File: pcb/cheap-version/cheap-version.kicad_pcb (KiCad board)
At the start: 4 copper layers, 100 x 100 mm, 169 parts, among them J201 UART / 3V3 logic, J301 SHT4x / XH 2.50, J302 FLOAT / 3.5 mm, J401 HRO TF-01A, J501 FAN1 / 3.5 mm, J511 FAN2 / 3.5 mm, J521 PUMP 24V / 6W, J601 PTC + / switched - (3.5 mm), J711 LED +/- (return isolated), J721 LED +/- (return isolated), J731 LED +/- (return isolated), J901 24V IN (KF301-5.0-2P), Q501 AO3400A, Q511 AO3400A, Q521 AO3422, Q601 IRL2505, Q711 BSC146N10LS5, Q721 BSC146N10LS5, SW201 RESET, SW202 BOOT, U101 ST1S10PHR, U201 ESP32-WROOM-32E-N4, U301 PCF8563T/5, U601 UCC27524ADR, U700 SN74LVC1G08DBVR, U710 AL8853S-13, U720 AL8853S-13, U902 ST1S14PHR, Y301 32.768k 12.5pF

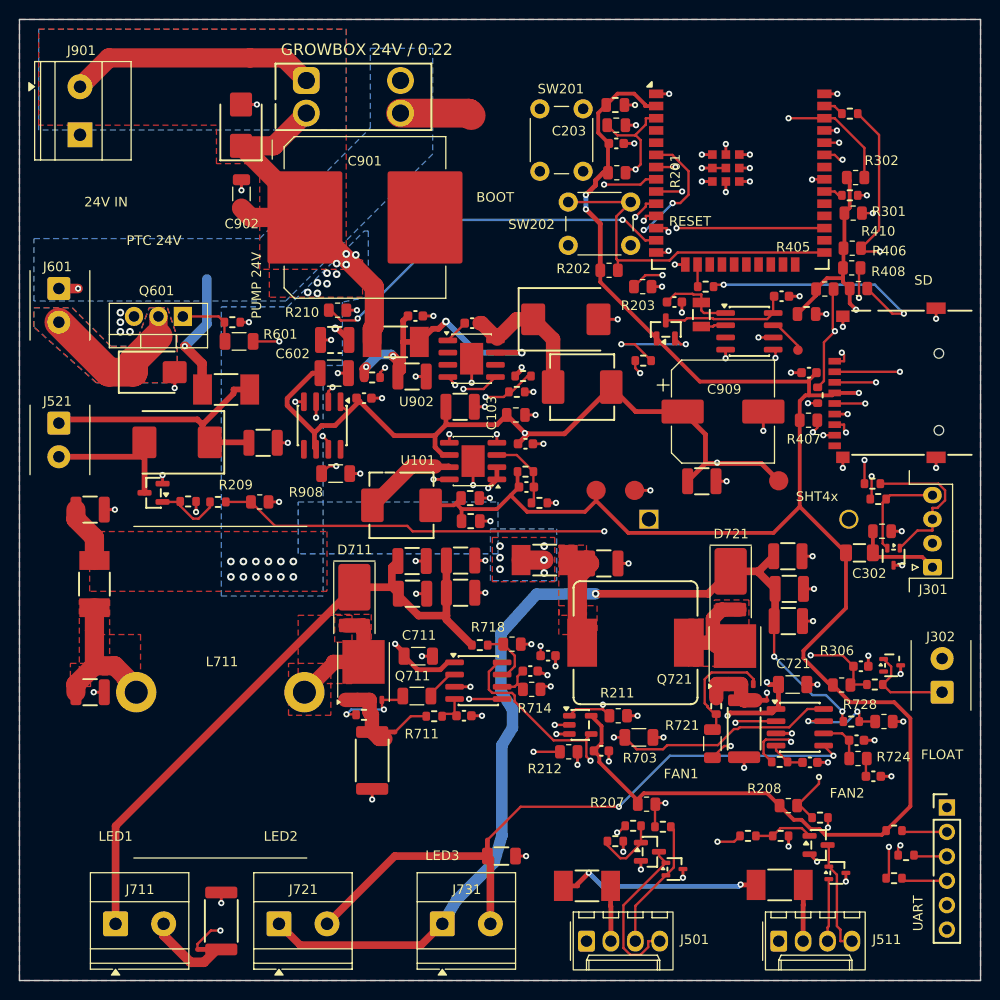
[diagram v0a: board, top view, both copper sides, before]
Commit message: cheap-version: JLCPCB DFM fixes (check_fab: 0 FAIL)
pcb/check_fab.py on the cheap-1 board found: three crossing vias on the
C901 pad (moved to 12 positions off the pad), nine same-net track corners
that skim a pad (merged by tools/fab_touchups.py, LED2_RETURN corner moved
onto the NT722 tie pad), silk strokes below 0.2 mm and silk within 0.15 mm
of pads, holes and vias (check_fab --fix-silk, then fix_silk.py again with
via-aware placement, 1.0 mm text, 0.2 mm strokes). The two silk labels with
the PCB_V1 revision now say CHEAP-1.

Result: check_fab 0 FAIL / 2 WARN (via ring 0.175 mm, same-net slits - same
as PCB_V1), DRC with .kicad_dru 0 violations, 0 unconnected.

Co-Authored-By: Claude Sonnet 5.5 <noreply@anthropic.com>
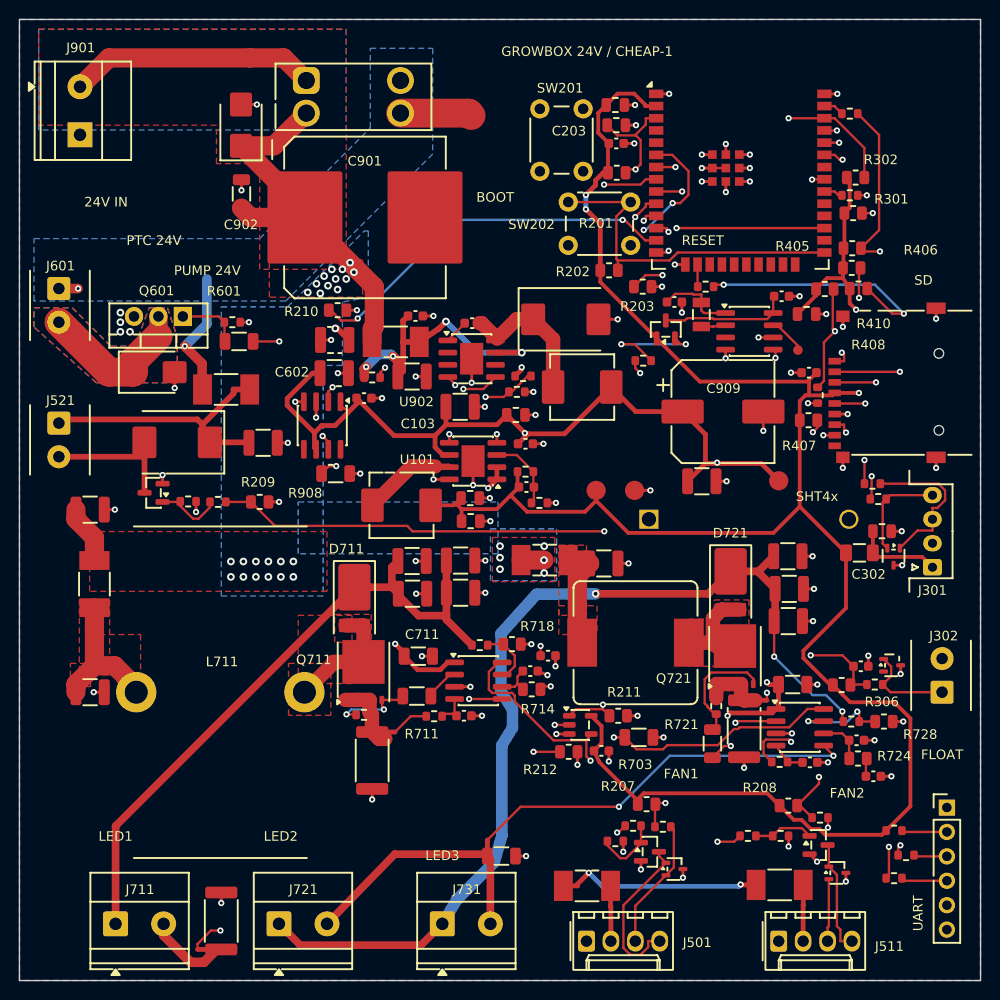
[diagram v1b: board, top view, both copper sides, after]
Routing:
- net +24V: vias 28 -> 30
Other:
- board text added: "GROWBOX 24V / CHEAP-1"
- board text added: "GROWBOX CHEAP-1 / BOTTOM"
- board text removed: "GROWBOX 0.22 / BOTTOM"
- board text removed: "GROWBOX 24V / 0.22"

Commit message: cheap-version: local HF bypass C911 at the ST1S14 VIN pin
The route from the input capacitors C905/C906 to U902 pin 7 is about 15 mm
of 0.6 mm copper with two vias, half of it on B.Cu above the +3V3 flood
instead of GND (hot-loop inductance 15 nH or more). C911, 100 nF 0603 from
stock (a copy of C907), now sits on the bottom side right under pins 6/7:
AUX_VIN pad on the existing B.Cu track, GND via beside it into In1, a
second AUX_VIN via next to pin 7 closes the loop (about 5 nH). Schematic
(generator), board (tools/add_c911.py), BOM (161 parts, 94 from stock),
DRC 0 / check_fab 0 FAIL.

Co-Authored-By: Claude Sonnet 5.5 <noreply@anthropic.com>
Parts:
- added C911: 100n 50V X7R, Capacitor_SMD:C_0603_1608Metric, B.Cu at (100.1, 85.1)
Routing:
- net GND: track 117.4 -> 118.4 mm, vias 103 -> 104
- net /InputPower/AUX_VIN: vias 5 -> 6
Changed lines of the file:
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@@
 		)
 	)
+	(footprint "Capacitor_SMD:C_0603_1608Metric"
+		(layer "B.Cu")
+		(at 100.1 85.1 -90)
+		(descr "Capacitor SMD 0603 (1608 Metric), square (rectangular) end terminal, IPC-7351 nominal, (Body size source: IPC-SM-782 page 76, https://www.pcb-3d.com/wordpress/wp-content/uploads/ipc-sm-782a_amendment_1_and_2.pdf)")
+		(tags "capacitor")
+		(property "Reference" "C911"
+			(at 0 0 90)
+			(layer "B.Fab")
+			(hide yes)
+			(effects
+				(font
+					(size 0.8 0.8)
+					(thickness 0.12)
+				)
+				(justify mirror)
+			)
+		)
+		(property "Value" "100n 50V X7R"
+			(at 0 -1.43 90)
+			(layer "B.Fab")
+			(hide yes)
+			(effects
+				(font
+					(size 1 1)
+					(thickness 0.15)
+				)
+				(justify mirror)
+			)
+		)
+		(property "Datasheet" ""
+			(at 0 0 90)
+			(layer "B.Fab")
+			(hide yes)
+			(effects
+				(font
+					(size 1.27 1.27)
+				)
+				(justify mirror)
+			)
+		)
+		(property "Description" ""
+			(at 0 0 90)
+			(layer "B.Fab")
+			(hide yes)
+			(effects
+				(font
+					(size 1.27 1.27)
+				)
+				(justify mirror)
+			)
+		)
+		(property "KiLib_Generator" "SMD_2terminal_chip_molded"
+			(at 0 0 90)
+			(layer "B.SilkS")
+			(hide yes)
+			(effects
+				(font
+					(size 1 1)
+					(thickness 0.15)
+				)
+				(justify mirror)
+			)
+		)
+		(property "Manufacturer" "Samsung"
+			(at 0 0 90)
+			(layer "B.SilkS")
+			(hide yes)
+			(effects
+				(font
+					(size 1.27 1.27)
+					(thickness 0.15)
+				)
+				(justify mirror)
+			)
+		)
+		(property "MPN" "CL10B104KB8NNNC"
+			(at 0 0 90)
+			(layer "B.SilkS")
+			(hide yes)
+			(effects
+				(font
+					(size 1.27 1.27)
+					(thickness 0.15)
+				)
+				(justify mirror)
+			)
+		)
+		(property "LCSC" "C1591"
+			(at 0 0 90)
+			(layer "B.SilkS")
+			(hide yes)
+			(effects
+				(font
+					(size 1.27 1.27)
+					(thickness 0.15)
+				)
+				(justify mirror)
+			)
+		)
+		(attr smd)
+		(duplicate_pad_numbers_are_jumpers no)
+		(fp_line
+			(start -0.14058 0.51)
+			(end 0.14058 0.51)
+			(stroke
+				(width 0.2)
+				(type solid)
+			)
+			(layer "B.SilkS")
+		)
+		(fp_line
+			(start -0.14058 -0.51)
+			(end 0.14058 -0.51)
+			(stroke
+				(width 0.2)
+				(type solid)
+			)
+			(layer "B.SilkS")
+		)
+		(fp_rect
+			(start -1.48 0.73)
+			(end 1.48 -0.73)
+			(stroke
+				(width 0.05)
+				(type solid)
+			)
+			(fill no)
+			(layer "B.CrtYd")
+		)
+		(fp_rect
+			(start -0.8 0.4)
+			(end 0.8 -0.4)
+			(stroke
+				(width 0.1)
+				(type solid)
+			)
+			(fill no)
+			(layer "B.Fab")
+		)
+		(fp_text user "${REFERENCE}"
+			(at 0 0 90)
+			(layer "B.Fab")
+			(effects
+				(font
+					(size 0.8 0.8)
+					(thickness 0.06)
+				)
+				(justify mirror)
+			)
+		)
+		(pad "1" smd roundrect
+			(at -0.775 0 270)
+			(size 0.9 0.95)
+			(layers "B.Cu" "B.Mask" "B.Paste")
+			(roundrect_rratio 0.25)
+			(net "/InputPower/AUX_VIN")
+		)
+		(pad "2" smd roundrect
+			(at 0.775 0 270)
+			(size 0.9 0.95)
+			(layers "B.Cu" "B.Mask" "B.Paste")
+			(roundrect_rratio 0.25)
+			(net "GND")
+		)
+		(embedded_fonts no)
+		(model "${KICAD10_3DMODEL_DIR}/Capacitor_SMD.3dshapes/C_0603_1608Metric.step"
+			(offset
+				(xyz 0 0 0)
+			)
+			(scale
+				(xyz 1 1 1)
+			)
+			(rotate
+				(xyz 0 0 0)
+			)
+		)
+	)
 	(footprint "Battery:BatteryHolder_MYOUNG_BS-07-A1BJ001_CR2032"
 		(layer "B.Cu")
@@
 	)
 	(via
+		(at 101.1 85.9)
+		(size 0.65)
+		(drill 0.3)
+		(layers "F.Cu" "B.Cu")
+		(locked yes)
+		(net "GND")
+	)
+	(via
 		(at 102.712499 137.05)
 		(size 0.65)
@@
 	)
 	(segment
+		(start 100.1 85.875)
+		(end 101.1 85.9)
+		(width 0.3)
+		(locked yes)
+		(layer "B.Cu")
+		(net "GND")
+	)
+	(segment
 		(start 108.975 106.25)
 		(end 109.325 106.6)
@@
 		(layers "F.Cu" "B.Cu")
 		(locked yes)
+		(net "/InputPower/AUX_VIN")
+	)
+	(via
+		(at 101.1 84.67)
+		(size 0.8)
+		(drill 0.4)
+		(layers "F.Cu" "B.Cu")
+		(locked yes)
